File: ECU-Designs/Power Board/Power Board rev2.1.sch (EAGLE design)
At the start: 52 parts, among them X2 MINIFIT_5566-6

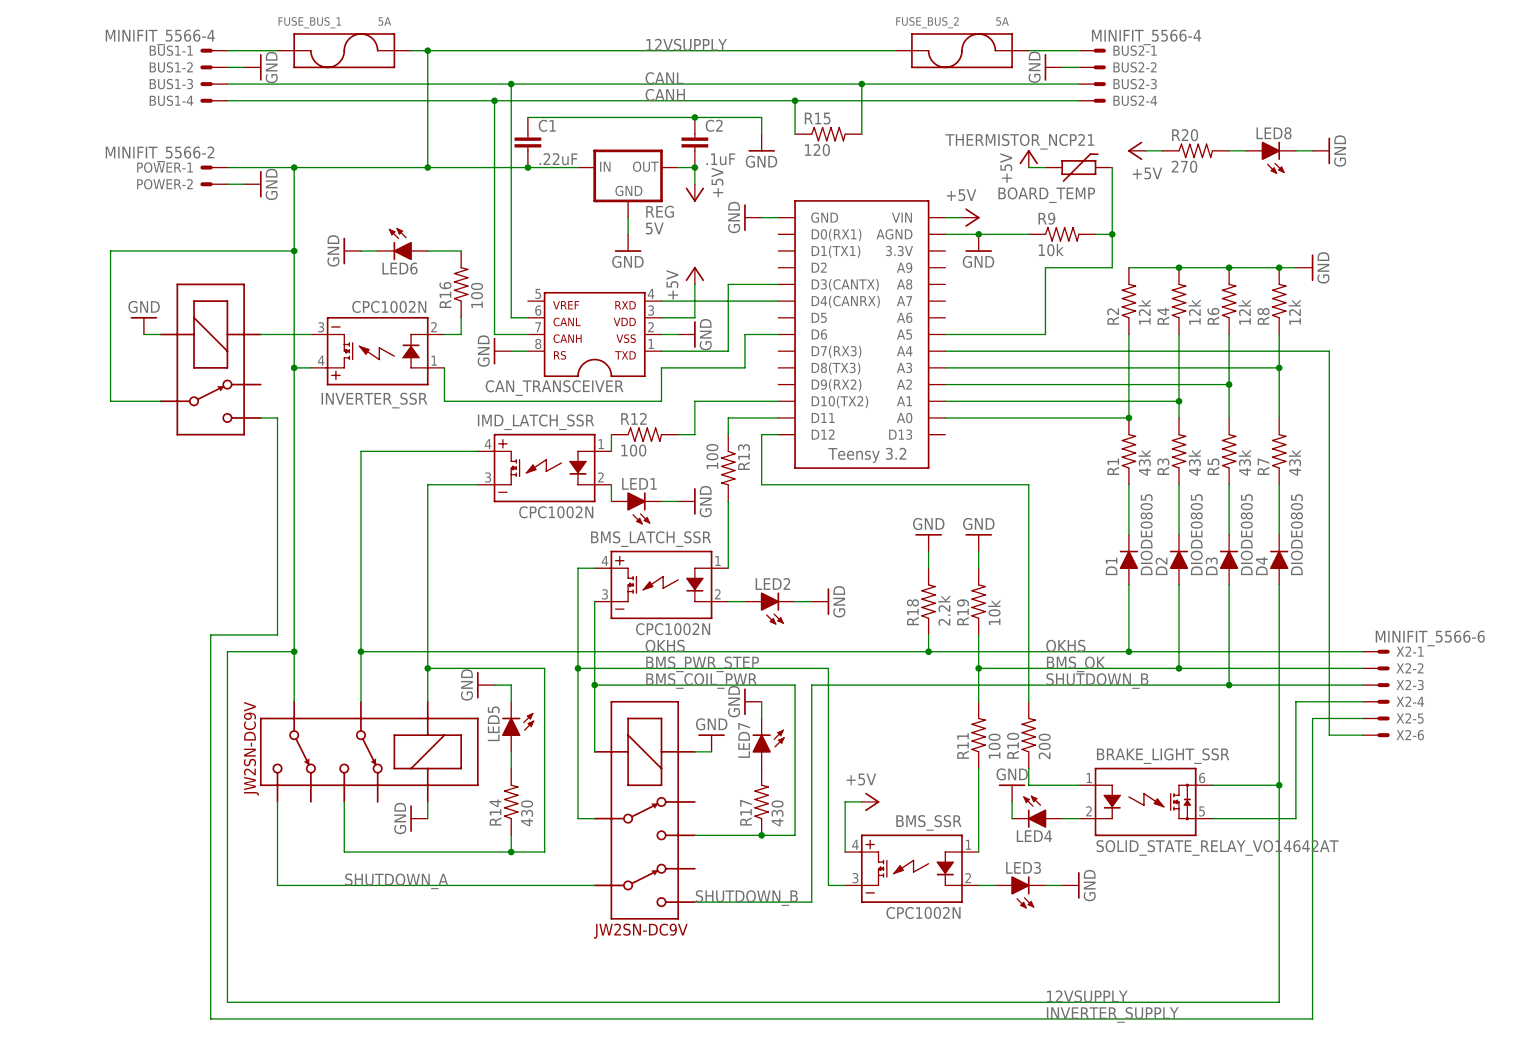
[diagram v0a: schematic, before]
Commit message: Add IMD driver SSR, use 12V Omron relay
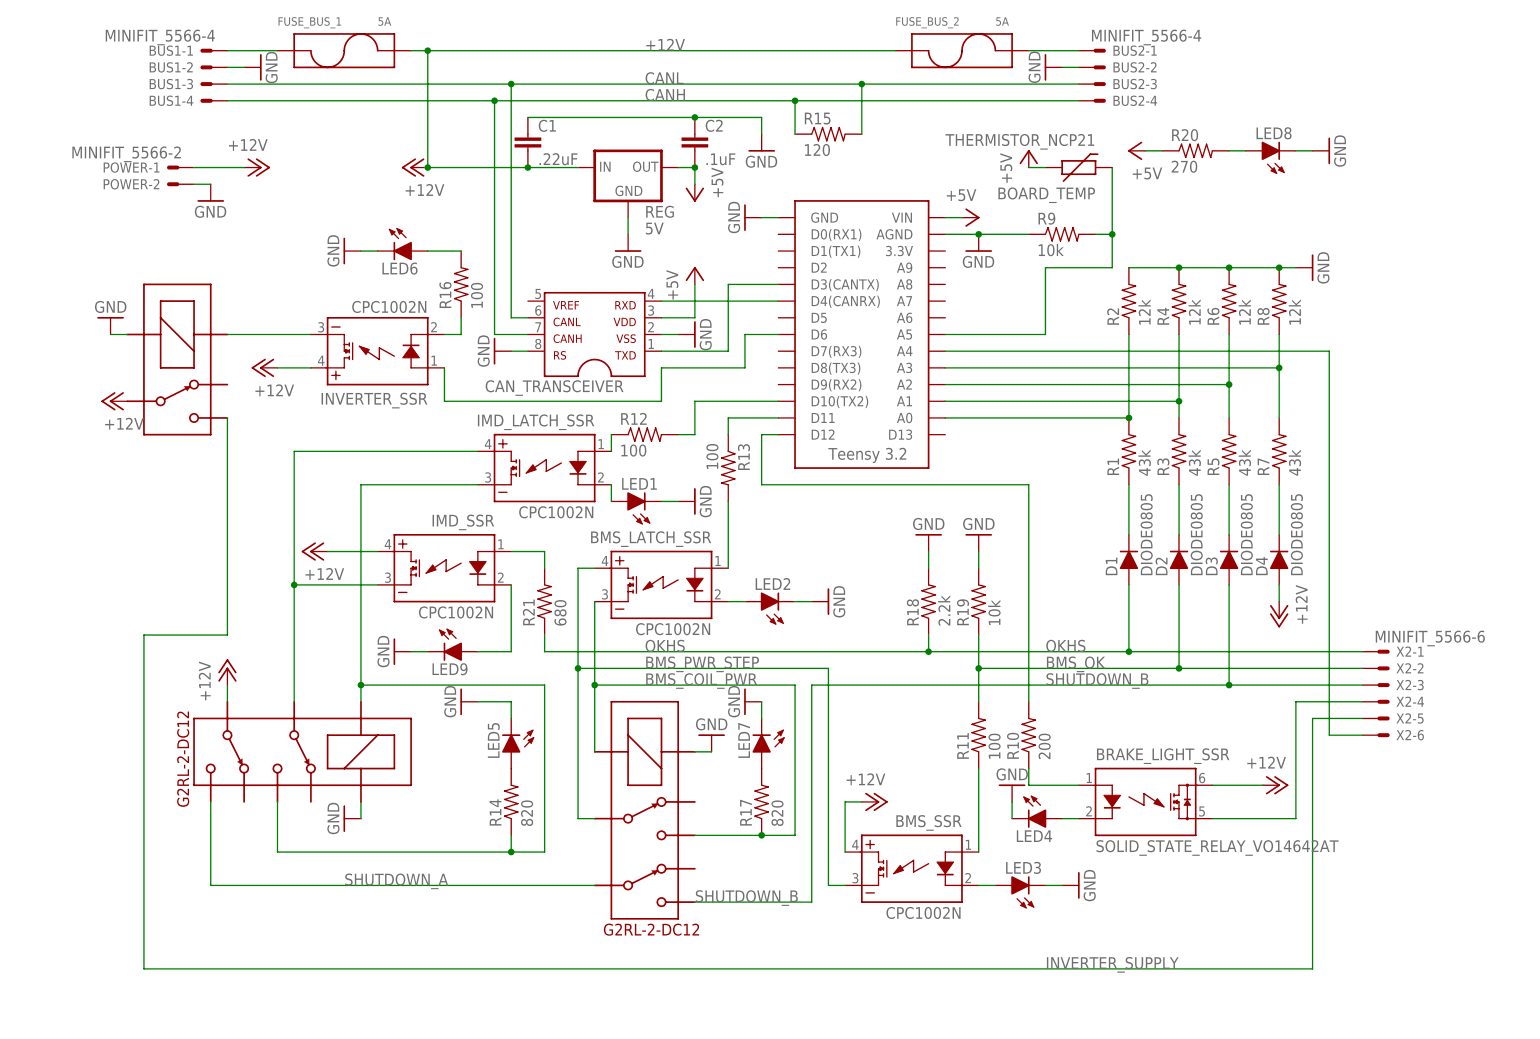
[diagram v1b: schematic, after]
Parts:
- added IMD_SSR: CPC1002N, HyTechDevices:CPC1002N
- added LED9: (no value), HyTechDevices:LED-0805
- added R21: 680, HyTechDevices:RESISTOR0805-RES
- IMD_SHUTDOWN, IMD_SHUTDOWN1: value DPDT_RELAY_PANASONIC_JW2SN-DC9V -> G2RL-2-DC12; device HyTechDevices:DPDT_RELAY_PANASONIC_JW2SN-DC9V -> HyTechDevices:G2RL-2-DC12
- R14, R17: value 430 -> 820
- U$1: value ORWH-SH-112D1F -> G5LE; device HyTechDevices:ORWH-SH-112D1F -> HyTechDevices:G5LE
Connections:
- removed net 12VSUPPLY: BRAKE_LIGHT_SSR.IO1, C1.2, D4.A, FUSE_BUS_1.P2, FUSE_BUS_2.P1, IMD_SHUTDOWN.6, INVERTER_SSR.DC+, POWER-1.S, REG.IN, U$1.P
- new net +12V: BMS_SSR.DC+, BRAKE_LIGHT_SSR.IO1, C1.2, D4.A, FUSE_BUS_1.P2, FUSE_BUS_2.P1, IMD_SHUTDOWN.6, IMD_SSR.DC+, INVERTER_SSR.DC+, POWER-1.S, REG.IN, U$1.P
- new net N$30: IMD_LATCH_SSR.DC+, IMD_SHUTDOWN.3, IMD_SSR.DC-
- new net N$31: IMD_SSR.CONTROL+, R21.2
- new net N$34: IMD_SSR.CONTROL-, LED9.A
- net +5V: no longer BMS_SSR.DC+
- net GND: now also LED9.C
- net OKHS: now also R21.1; no longer IMD_LATCH_SSR.DC+, IMD_SHUTDOWN.3
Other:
- moved on the sheet: LED5, POWER-1, POWER-2

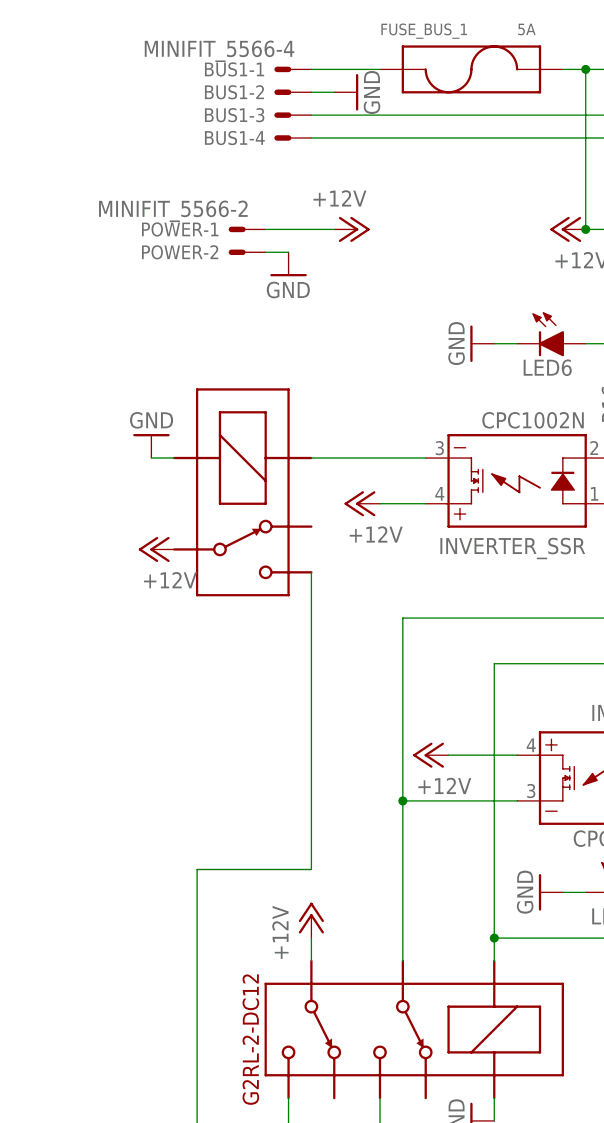
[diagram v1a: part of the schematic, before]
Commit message: Add separate shutdown circuit power to board
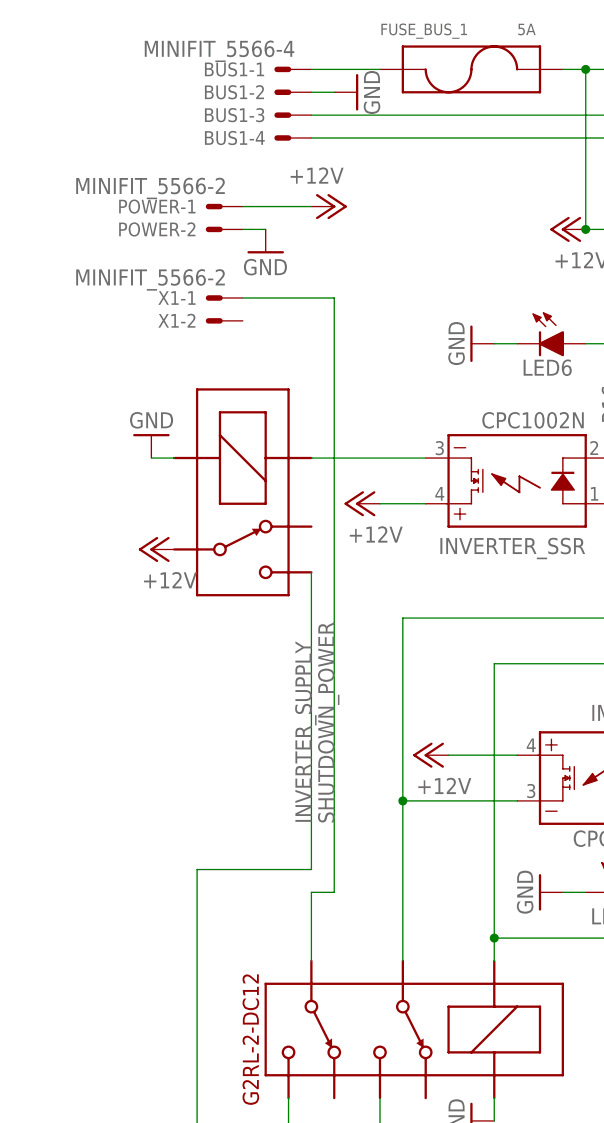
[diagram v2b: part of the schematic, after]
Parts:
- added X1: MINIFIT_5566-2, HyTechDevices:MINIFIT_5566-2
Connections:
- new net SHUTDOWN_POWER: IMD_SHUTDOWN.6, X1-1.S
- net +12V: no longer IMD_SHUTDOWN.6
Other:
- moved on the sheet: POWER-1, POWER-2
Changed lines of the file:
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@@
 <part name="P+9" library="supply1" deviceset="+12V" device=""/>
 <part name="P+10" library="supply1" deviceset="+12V" device=""/>
-<part name="P+11" library="supply1" deviceset="+12V" device=""/>
 <part name="P+12" library="supply1" deviceset="+12V" device=""/>
 <part name="P+13" library="supply1" deviceset="+12V" device=""/>
 <part name="P+14" library="supply1" deviceset="+12V" device=""/>
 <part name="P+5" library="supply1" deviceset="+12V" device=""/>
+<part name="X1" library="HyTechDevices" deviceset="MINIFIT_5566-2" device=""/>
 </parts>
 <sheets>
@@
 <instance part="IMD_SHUTDOWN" gate="G$1" x="27.94" y="22.86" rot="R180"/>
 <instance part="GND13" gate="1" x="20.32" y="10.16" rot="R270"/>
-<instance part="POWER" gate="-2" x="-5.08" y="106.68" rot="MR0"/>
-<instance part="POWER" gate="-1" x="-5.08" y="109.22" rot="MR0"/>
+<instance part="POWER" gate="-2" x="-7.62" y="109.22" rot="MR0"/>
+<instance part="POWER" gate="-1" x="-7.62" y="111.76" rot="MR0"/>
 <instance part="BUS2" gate="-1" x="134.62" y="127"/>
 <instance part="BUS2" gate="-2" x="134.62" y="124.46"/>
@@
 <instance part="FUSE_BUS_1" gate="G$1" x="20.32" y="127"/>
 <instance part="FUSE_BUS_2" gate="G$1" x="114.3" y="127"/>
-<instance part="GND2" gate="1" x="0" y="104.14"/>
+<instance part="GND2" gate="1" x="-2.54" y="106.68"/>
 <instance part="GND15" gate="1" x="7.62" y="124.46" rot="R90"/>
 <instance part="GND16" gate="1" x="127" y="124.46" rot="R270"/>
@@
 <instance part="GND24" gate="1" x="27.94" y="35.56" rot="R270"/>
 <instance part="R21" gate="G$1" x="50.8" y="43.18" rot="R90"/>
-<instance part="P+7" gate="1" x="7.62" y="109.22" rot="R270"/>
+<instance part="P+7" gate="1" x="5.08" y="111.76" rot="R270"/>
 <instance part="P+8" gate="1" x="-15.24" y="73.66" rot="R90"/>
 <instance part="P+9" gate="1" x="7.62" y="78.74" rot="R90"/>
 <instance part="P+10" gate="1" x="15.24" y="50.8" rot="R90"/>
-<instance part="P+11" gate="1" x="2.54" y="33.02"/>
 <instance part="P+12" gate="1" x="162.56" y="15.24" rot="R270"/>
 <instance part="P+13" gate="1" x="162.56" y="40.64" rot="R180"/>
 <instance part="P+14" gate="1" x="30.48" y="109.22" rot="R90"/>
 <instance part="P+5" gate="1" x="101.6" y="12.7" rot="R270"/>
+<instance part="X1" gate="-2" x="-7.62" y="99.06" rot="MR0"/>
+<instance part="X1" gate="-1" x="-7.62" y="101.6" rot="MR0"/>
 </instances>
 <busses>
@@
 <pinref part="POWER" gate="-2" pin="S"/>
 <pinref part="GND2" gate="1" pin="GND"/>
-<wire x1="0" y1="106.68" x2="-2.54" y2="106.68" width="0.1524" layer="91"/>
+<wire x1="-2.54" y1="109.22" x2="-5.08" y2="109.22" width="0.1524" layer="91"/>
 </segment>
 <segment>
@@
 <wire x1="167.64" y1="25.4" x2="175.26" y2="25.4" width="0.1524" layer="91"/>
 <label x="127" y="-12.7" size="1.778" layer="95"/>
+<label x="2.54" y="43.18" size="1.778" layer="95" rot="R90"/>
 </segment>
 </net>
@@
 <segment>
 <pinref part="POWER" gate="-1" pin="S"/>
-<wire x1="5.08" y1="109.22" x2="-2.54" y2="109.22" width="0.1524" layer="91"/>
+<wire x1="2.54" y1="111.76" x2="-5.08" y2="111.76" width="0.1524" layer="91"/>
 <pinref part="P+7" gate="1" pin="+12V"/>
 </segment>
@@
 <wire x1="25.4" y1="50.8" x2="17.78" y2="50.8" width="0.1524" layer="91"/>
 <pinref part="P+10" gate="1" pin="+12V"/>
-</segment>
-<segment>
-<pinref part="IMD_SHUTDOWN" gate="G$1" pin="6"/>
-<pinref part="P+11" gate="1" pin="+12V"/>
-<wire x1="2.54" y1="30.48" x2="2.54" y2="27.94" width="0.1524" layer="91"/>
 </segment>
 <segment>
@@
 </segment>
 </net>
+<net name="SHUTDOWN_POWER" class="0">
+<segment>
+<wire x1="5.08" y1="101.6" x2="5.08" y2="35.56" width="0.1524" layer="91"/>
+<pinref part="IMD_SHUTDOWN" gate="G$1" pin="6"/>
+<wire x1="5.08" y1="35.56" x2="2.54" y2="35.56" width="0.1524" layer="91"/>
+<wire x1="2.54" y1="35.56" x2="2.54" y2="27.94" width="0.1524" layer="91"/>
+<pinref part="X1" gate="-1" pin="S"/>
+<wire x1="-5.08" y1="101.6" x2="5.08" y2="101.6" width="0.1524" layer="91"/>
+<label x="5.08" y="43.18" size="1.778" layer="95" rot="R90"/>
+</segment>
+</net>
